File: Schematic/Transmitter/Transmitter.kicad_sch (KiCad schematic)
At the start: 4 parts, among them J2 Remote Umbilical, U1 Mini360, U2 RFM69HW, U3 BP

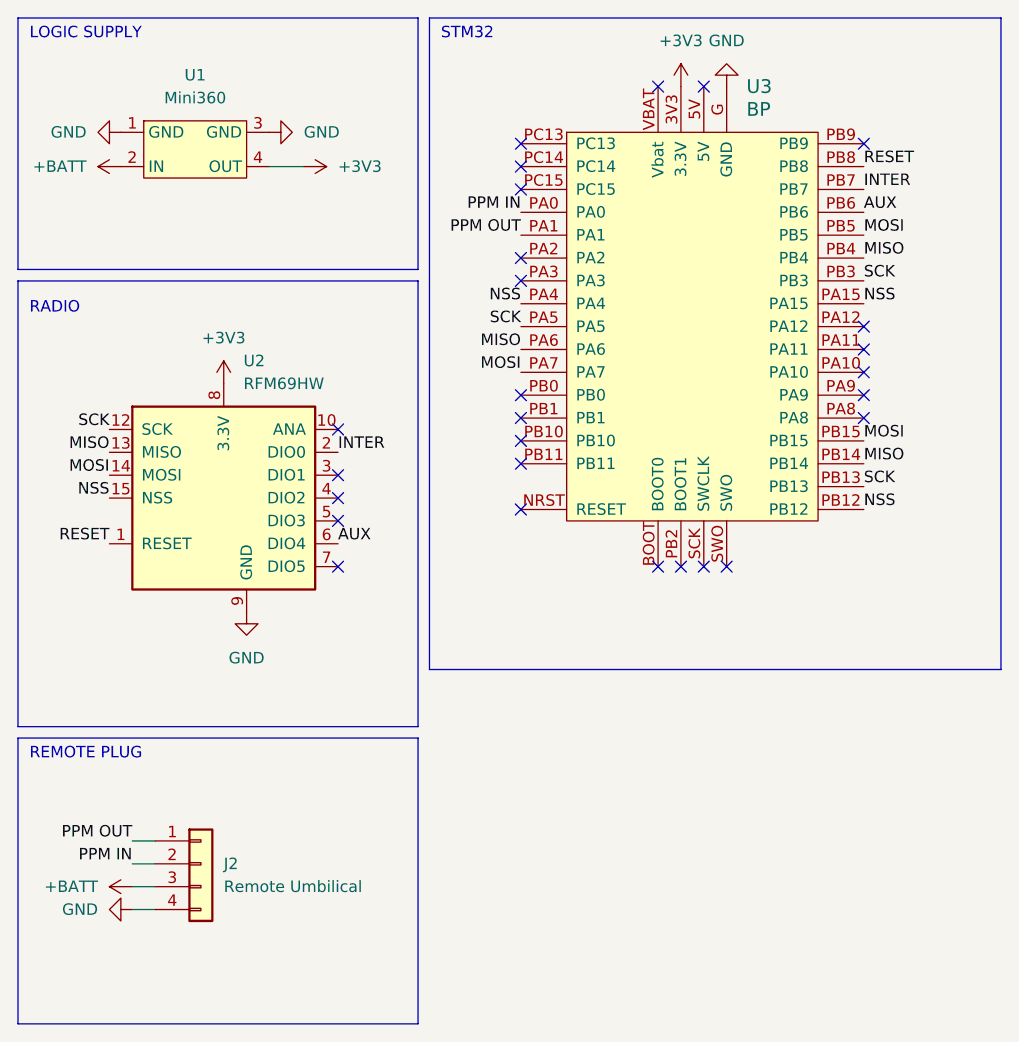
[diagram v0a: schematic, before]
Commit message: Add transmitter PCB
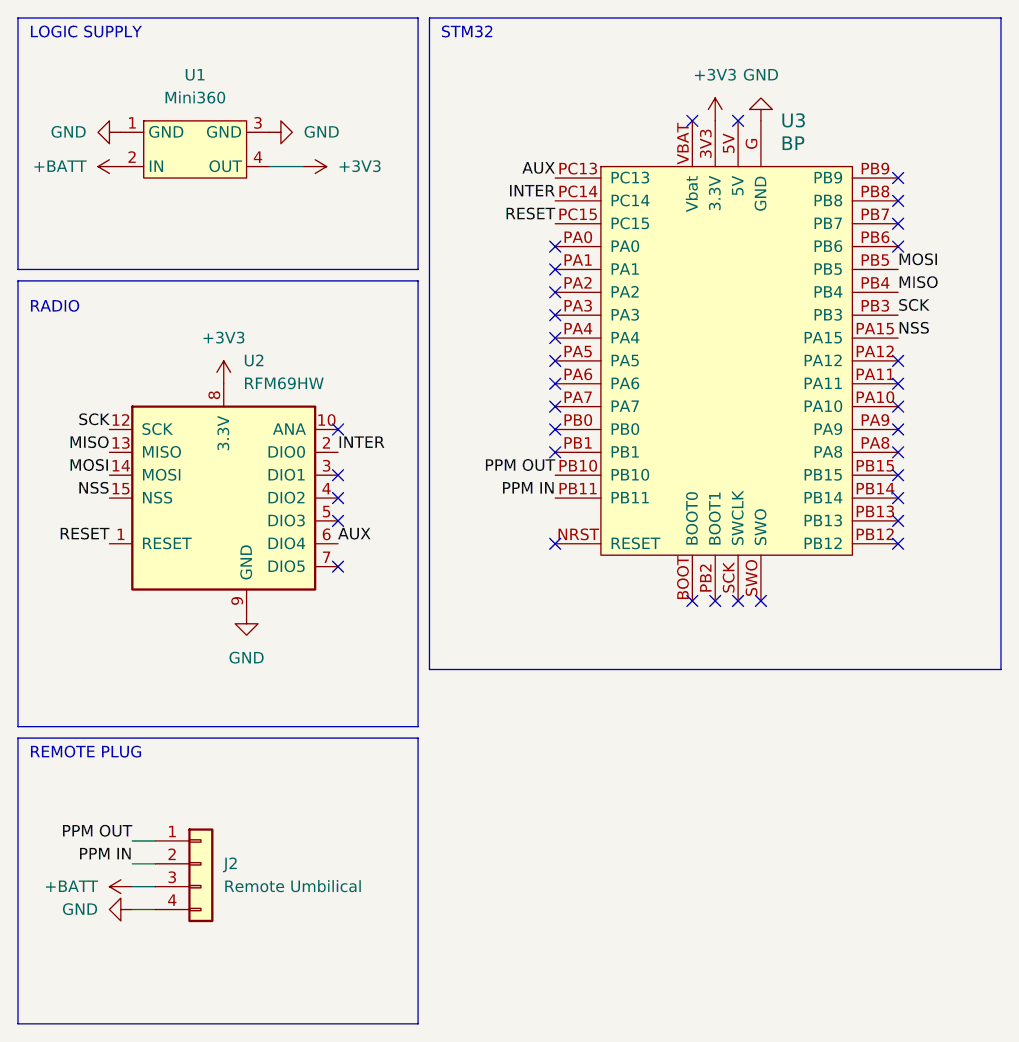
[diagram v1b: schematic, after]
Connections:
- net AUX: now also U3.PC13; no longer U3.PB6
- net INTER: now also U3.PC14; no longer U3.PB7
- net MISO: no longer U3.PA6, U3.PB14
- net MOSI: no longer U3.PA7, U3.PB15
- net NSS: no longer U3.PA4, U3.PB12
- net PPM IN: now also U3.PB11; no longer U3.PA0
- net PPM OUT: now also U3.PB10; no longer U3.PA1
- net RESET: now also U3.PC15; no longer U3.PB8
- net SCK: no longer U3.PA5, U3.PB13
- no-connect marks 27 -> 35
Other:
- moved on the sheet: U3
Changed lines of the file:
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@@
 (kicad_sch (version 20230121) (generator eeschema)
   (paper "A4")
-  (no_connect (at 115.57 71.12))
-  (no_connect (at 92.71 34.29))
+  (no_connect (at 119.38 82.55))
+  (no_connect (at 119.38 74.93))
+  (no_connect (at 96.52 38.1))
   (no_connect (at 57.15 77.47))
-  (no_connect (at 97.79 87.63))
-  (no_connect (at 92.71 87.63))
+  (no_connect (at 119.38 46.99))
+  (no_connect (at 101.6 91.44))
+  (no_connect (at 119.38 49.53))
+  (no_connect (at 96.52 91.44))
   (no_connect (at 57.15 82.55))
-  (no_connect (at 77.47 76.2))
-  (no_connect (at 115.57 63.5))
-  (no_connect (at 77.47 45.72))
-  (no_connect (at 95.25 87.63))
-  (no_connect (at 97.79 34.29))
-  (no_connect (at 77.47 55.88))
-  (no_connect (at 115.57 66.04))
-  (no_connect (at 77.47 81.28))
-  (no_connect (at 77.47 68.58))
-  (no_connect (at 77.47 43.18))
-  (no_connect (at 115.57 60.96))
+  (no_connect (at 119.38 67.31))
+  (no_connect (at 119.38 52.07))
+  (no_connect (at 99.06 91.44))
+  (no_connect (at 119.38 85.09))
+  (no_connect (at 101.6 38.1))
+  (no_connect (at 81.28 59.69))
+  (no_connect (at 119.38 69.85))
+  (no_connect (at 81.28 85.09))
+  (no_connect (at 81.28 62.23))
+  (no_connect (at 81.28 72.39))
+  (no_connect (at 81.28 54.61))
+  (no_connect (at 119.38 77.47))
+  (no_connect (at 119.38 64.77))
   (no_connect (at 57.15 80.01))
-  (no_connect (at 115.57 40.64))
-  (no_connect (at 100.33 87.63))
-  (no_connect (at 115.57 68.58))
-  (no_connect (at 77.47 40.64))
+  (no_connect (at 119.38 44.45))
+  (no_connect (at 81.28 64.77))
+  (no_connect (at 81.28 69.85))
+  (no_connect (at 81.28 67.31))
+  (no_connect (at 104.14 91.44))
+  (no_connect (at 119.38 80.01))
+  (no_connect (at 81.28 52.07))
+  (no_connect (at 119.38 72.39))
   (no_connect (at 57.15 87.63))
-  (no_connect (at 77.47 53.34))
+  (no_connect (at 81.28 57.15))
   (no_connect (at 57.15 72.39))
-  (no_connect (at 77.47 71.12))
-  (no_connect (at 77.47 73.66))
+  (no_connect (at 81.28 74.93))
   (wire (pts (xy 34.29 118.11) (xy 36.83 118.11))
     (stroke (width 0) (type default))
@@
     (effects (font (size 1.27 1.27)) (justify left bottom))
   )
-  (label "PPM OUT" (at 77.47 50.8 180) (fields_autoplaced)
-    (effects (font (size 1.27 1.27)) (justify right bottom))
-  )
-  (label "MOSI" (at 115.57 50.8 0) (fields_autoplaced)
+  (label "PPM OUT" (at 81.28 77.47 180) (fields_autoplaced)
+    (effects (font (size 1.27 1.27)) (justify right bottom))
+  )
+  (label "MOSI" (at 119.38 54.61 0) (fields_autoplaced)
     (effects (font (size 1.27 1.27)) (justify left bottom))
   )
@@
     (effects (font (size 1.27 1.27)) (justify right bottom))
   )
-  (label "PPM IN" (at 77.47 48.26 180) (fields_autoplaced)
-    (effects (font (size 1.27 1.27)) (justify right bottom))
-  )
-  (label "SCK" (at 115.57 55.88 0) (fields_autoplaced)
-    (effects (font (size 1.27 1.27)) (justify left bottom))
-  )
-  (label "AUX" (at 115.57 48.26 0) (fields_autoplaced)
-    (effects (font (size 1.27 1.27)) (justify left bottom))
+  (label "PPM IN" (at 81.28 80.01 180) (fields_autoplaced)
+    (effects (font (size 1.27 1.27)) (justify right bottom))
+  )
+  (label "SCK" (at 119.38 59.69 0) (fields_autoplaced)
+    (effects (font (size 1.27 1.27)) (justify left bottom))
+  )
+  (label "AUX" (at 81.28 44.45 180) (fields_autoplaced)
+    (effects (font (size 1.27 1.27)) (justify right bottom))
   )
   (label "PPM OUT" (at 34.29 118.11 180) (fields_autoplaced)
@@
     (effects (font (size 1.27 1.27)) (justify right bottom))
   )
-  (label "MOSI" (at 77.47 66.04 180) (fields_autoplaced)
-    (effects (font (size 1.27 1.27)) (justify right bottom))
-  )
-  (label "NSS" (at 115.57 81.28 0) (fields_autoplaced)
-    (effects (font (size 1.27 1.27)) (justify left bottom))
-  )
-  (label "MOSI" (at 115.57 73.66 0) (fields_autoplaced)
-    (effects (font (size 1.27 1.27)) (justify left bottom))
-  )
-  (label "MISO" (at 115.57 76.2 0) (fields_autoplaced)
-    (effects (font (size 1.27 1.27)) (justify left bottom))
-  )
-  (label "MISO" (at 77.47 63.5 180) (fields_autoplaced)
-    (effects (font (size 1.27 1.27)) (justify right bottom))
-  )
-  (label "MISO" (at 115.57 53.34 0) (fields_autoplaced)
+  (label "MISO" (at 119.38 57.15 0) (fields_autoplaced)
     (effects (font (size 1.27 1.27)) (justify left bottom))
   )
@@
     (effects (font (size 1.27 1.27)) (justify left bottom))
   )
-  (label "INTER" (at 115.57 45.72 0) (fields_autoplaced)
-    (effects (font (size 1.27 1.27)) (justify left bottom))
-  )
-  (label "NSS" (at 115.57 58.42 0) (fields_autoplaced)
+  (label "INTER" (at 81.28 46.99 180) (fields_autoplaced)
+    (effects (font (size 1.27 1.27)) (justify right bottom))
+  )
+  (label "NSS" (at 119.38 62.23 0) (fields_autoplaced)
     (effects (font (size 1.27 1.27)) (justify left bottom))
   )
@@
     (effects (font (size 1.27 1.27)) (justify right bottom))
   )
-  (label "SCK" (at 115.57 78.74 0) (fields_autoplaced)
-    (effects (font (size 1.27 1.27)) (justify left bottom))
-  )
-  (label "SCK" (at 77.47 60.96 180) (fields_autoplaced)
-    (effects (font (size 1.27 1.27)) (justify right bottom))
-  )
   (label "MISO" (at 31.75 74.93 180) (fields_autoplaced)
     (effects (font (size 1.27 1.27)) (justify right bottom))
   )
-  (label "NSS" (at 77.47 58.42 180) (fields_autoplaced)
-    (effects (font (size 1.27 1.27)) (justify right bottom))
-  )
-  (label "RESET" (at 115.57 43.18 0) (fields_autoplaced)
-    (effects (font (size 1.27 1.27)) (justify left bottom))
-  )
-  (symbol (lib_id "My_Library:STM32 Bluepill") (at 96.52 60.96 0) (unit 1)
-    (in_bom yes) (on_board yes) (dnp no) (fields_autoplaced)
-    (property "Reference" "U3" (at 102.5241 34.29 0)
+  (label "RESET" (at 81.28 49.53 180) (fields_autoplaced)
+    (effects (font (size 1.27 1.27)) (justify right bottom))
+  )
+  (symbol (lib_id "My_Library:STM32 Bluepill") (at 100.33 64.77 0) (unit 1)
+    (in_bom yes) (on_board yes) (dnp no) (fields_autoplaced)
+    (property "Reference" "U3" (at 106.3341 38.1 0)
       (effects (font (size 1.524 1.524)) (justify left))
     )
-    (property "Value" "BP" (at 102.5241 36.83 0)
+    (property "Value" "BP" (at 106.3341 40.64 0)
       (effects (font (size 1.524 1.524)) (justify left))
     )
-    (property "Footprint" "My_Library:blue_pill" (at 114.3 24.13 0)
+    (property "Footprint" "My_Library:blue_pill" (at 118.11 27.94 0)
       (effects (font (size 1.524 1.524)) hide)
     )
-    (property "Datasheet" "https://www.electronicshub.org/getting-started-with-stm32f103c8t6-blue-pill/" (at 100.33 20.32 0)
+    (property "Datasheet" "https://www.electronicshub.org/getting-started-with-stm32f103c8t6-blue-pill/" (at 104.14 24.13 0)
       (effects (font (size 1.524 1.524)) hide)
     )
@@
     )
   )
-  (symbol (lib_id "power:+3V3") (at 95.25 34.29 0) (unit 1)
-    (in_bom yes) (on_board yes) (dnp no) (fields_autoplaced)
-    (property "Reference" "#PWR06" (at 95.25 38.1 0)
-      (effects (font (size 1.27 1.27)) hide)
-    )
-    (property "Value" "+3V3" (at 95.25 29.21 0)
+  (symbol (lib_id "power:+3V3") (at 99.06 38.1 0) (unit 1)
+    (in_bom yes) (on_board yes) (dnp no) (fields_autoplaced)
+    (property "Reference" "#PWR06" (at 99.06 41.91 0)
+      (effects (font (size 1.27 1.27)) hide)
+    )
+    (property "Value" "+3V3" (at 99.06 33.02 0)
       (effects (font (size 1.27 1.27)))
     )
-    (property "Footprint" "" (at 95.25 34.29 0)
-      (effects (font (size 1.27 1.27)) hide)
-    )
-    (property "Datasheet" "" (at 95.25 34.29 0)
+    (property "Footprint" "" (at 99.06 38.1 0)
+      (effects (font (size 1.27 1.27)) hide)
+    )
+    (property "Datasheet" "" (at 99.06 38.1 0)
       (effects (font (size 1.27 1.27)) hide)
     )
@@
     )
   )
-  (symbol (lib_id "power:GND") (at 100.33 34.29 180) (unit 1)
-    (in_bom yes) (on_board yes) (dnp no) (fields_autoplaced)
-    (property "Reference" "#PWR07" (at 100.33 27.94 0)
-      (effects (font (size 1.27 1.27)) hide)
-    )
-    (property "Value" "GND" (at 100.33 29.21 0)
+  (symbol (lib_id "power:GND") (at 104.14 38.1 180) (unit 1)
+    (in_bom yes) (on_board yes) (dnp no) (fields_autoplaced)
+    (property "Reference" "#PWR07" (at 104.14 31.75 0)
+      (effects (font (size 1.27 1.27)) hide)
+    )
+    (property "Value" "GND" (at 104.14 33.02 0)
       (effects (font (size 1.27 1.27)))
     )
-    (property "Footprint" "" (at 100.33 34.29 0)
-      (effects (font (size 1.27 1.27)) hide)
-    )
-    (property "Datasheet" "" (at 100.33 34.29 0)
-      (effects (font (size 1.27 1.27)) hide)
-    )
+    (property "Footprint" "" (at 104.14 38.1 0)
+      (effects (font (size 1.27 1.27)) hide)
+    )
+    (property "Datasheet" "" (at 104.14 38.1 0)
+      (effects (font (size 1.27 1.27)) hide)
+    )

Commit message: Work on transmitter breakout
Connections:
- net MISO: now also U3.PA6; no longer U3.PB4
- net MOSI: now also U3.PA7; no longer U3.PB5
- net NSS: now also U3.PA4; no longer U3.PA15
- net SCK: now also U3.PA5; no longer U3.PB3
- no-connect marks 35 -> 31
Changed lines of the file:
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@@
   (no_connect (at 119.38 69.85))
   (no_connect (at 81.28 85.09))
-  (no_connect (at 81.28 62.23))
   (no_connect (at 81.28 72.39))
   (no_connect (at 81.28 54.61))
@@
   (no_connect (at 57.15 80.01))
   (no_connect (at 119.38 44.45))
-  (no_connect (at 81.28 64.77))
-  (no_connect (at 81.28 69.85))
-  (no_connect (at 81.28 67.31))
   (no_connect (at 104.14 91.44))
   (no_connect (at 119.38 80.01))
@@
     (effects (font (size 1.27 1.27)) (justify right bottom))
   )
-  (label "MOSI" (at 119.38 54.61 0) (fields_autoplaced)
-    (effects (font (size 1.27 1.27)) (justify left bottom))
+  (label "MOSI" (at 81.28 69.85 180) (fields_autoplaced)
+    (effects (font (size 1.27 1.27)) (justify right bottom))
   )
   (label "INTER" (at 57.15 74.93 0) (fields_autoplaced)
@@
     (effects (font (size 1.27 1.27)) (justify right bottom))
   )
-  (label "SCK" (at 119.38 59.69 0) (fields_autoplaced)
-    (effects (font (size 1.27 1.27)) (justify left bottom))
+  (label "SCK" (at 81.28 64.77 180) (fields_autoplaced)
+    (effects (font (size 1.27 1.27)) (justify right bottom))
   )
   (label "AUX" (at 81.28 44.45 180) (fields_autoplaced)
@@
     (effects (font (size 1.27 1.27)) (justify right bottom))
   )
-  (label "MISO" (at 119.38 57.15 0) (fields_autoplaced)
-    (effects (font (size 1.27 1.27)) (justify left bottom))
+  (label "MISO" (at 81.28 67.31 180) (fields_autoplaced)
+    (effects (font (size 1.27 1.27)) (justify right bottom))
   )
   (label "AUX" (at 57.15 85.09 0) (fields_autoplaced)
@@
     (effects (font (size 1.27 1.27)) (justify right bottom))
   )
-  (label "NSS" (at 119.38 62.23 0) (fields_autoplaced)
-    (effects (font (size 1.27 1.27)) (justify left bottom))
+  (label "NSS" (at 81.28 62.23 180) (fields_autoplaced)
+    (effects (font (size 1.27 1.27)) (justify right bottom))
   )
   (label "MOSI" (at 31.75 77.47 180) (fields_autoplaced)
